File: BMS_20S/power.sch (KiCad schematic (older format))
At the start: 40 parts, among them U301 LMC7660, U302 LMC7660, U303 LM317_3PinPackage, U304 LMC7660, U305 LMC7660

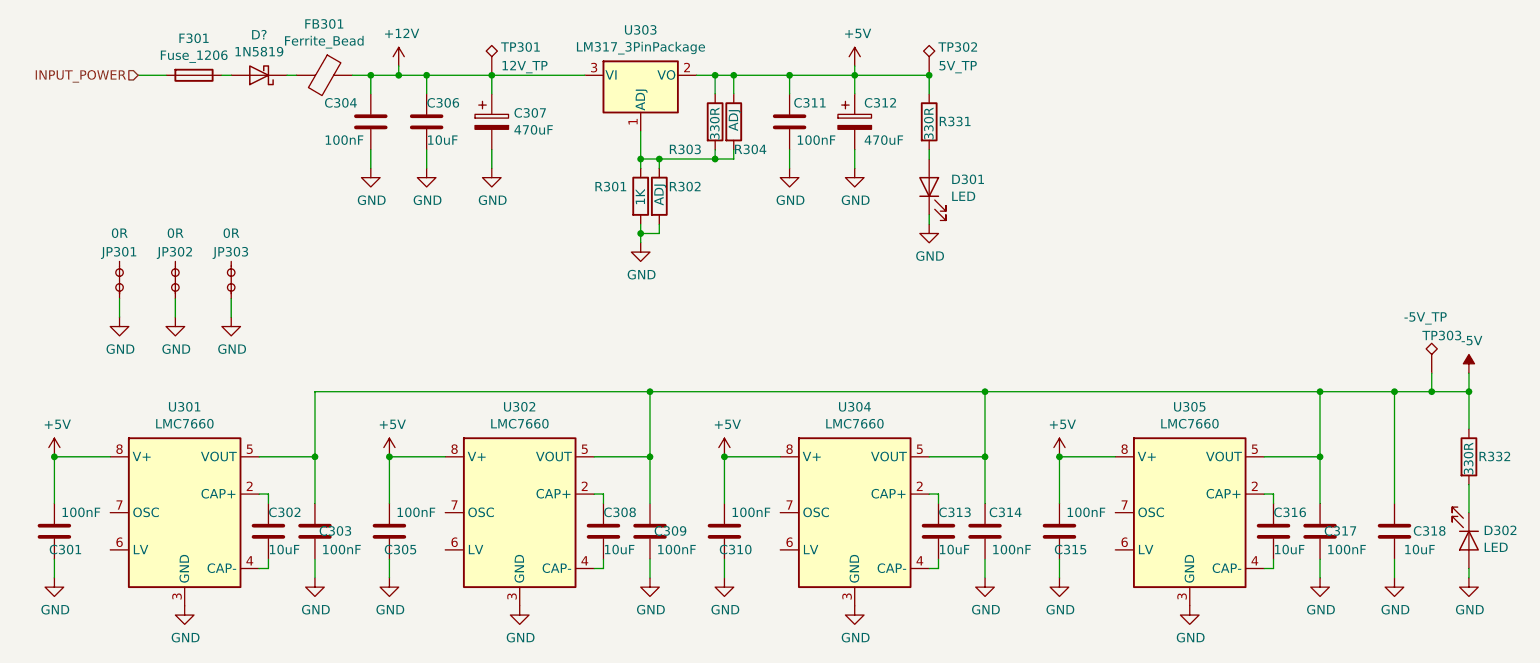
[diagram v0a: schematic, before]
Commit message: add current sense block to the schematic
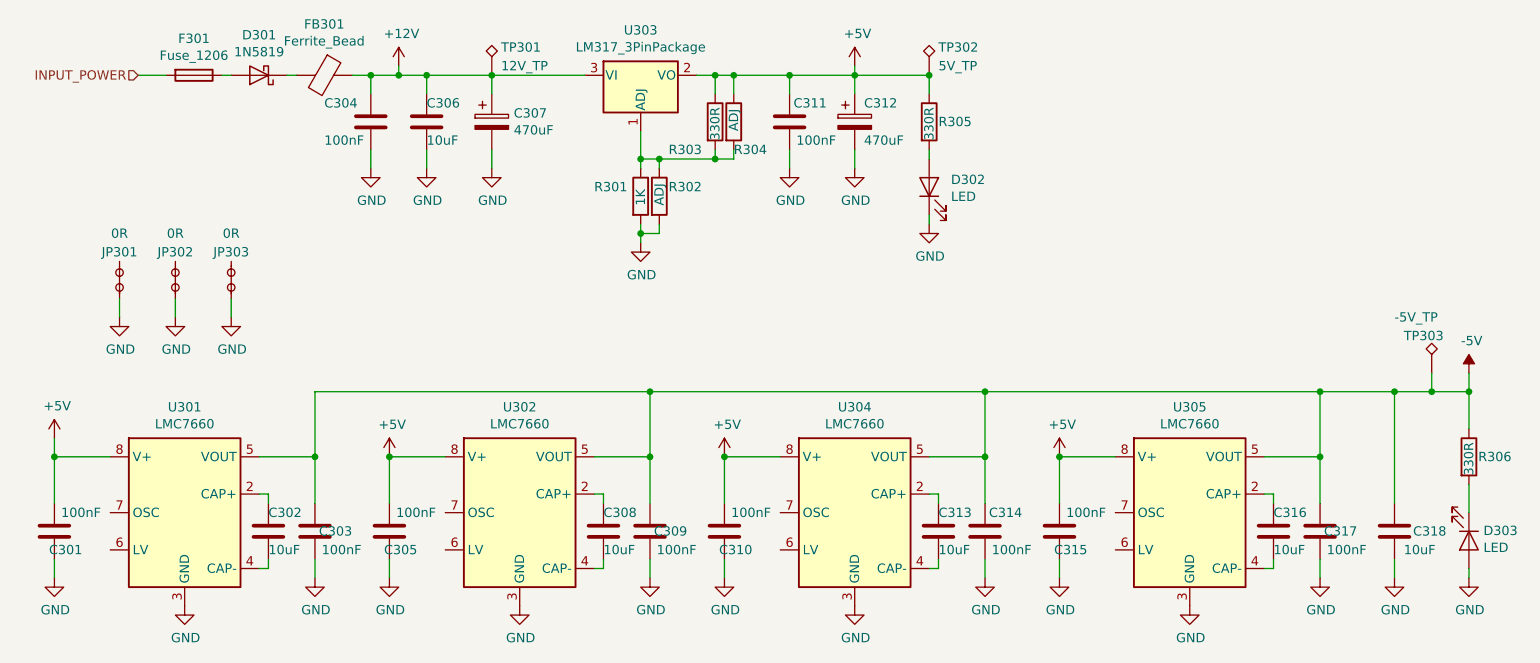
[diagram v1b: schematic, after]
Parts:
- gave numbers to parts that had none: 1
- renumbered D301 to D302, D302 to D303, R331 to R305, R332 to R306
